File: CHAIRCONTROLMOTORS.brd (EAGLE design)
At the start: 110 x 115 mm, 57 parts, among them IC5 MCP2551, IC6 MCP2515, IC7 ATMEGA32U4NT-TQFP, J1 LEFT MOTOR, J10 XTXX-30F, J11 USB-B-PTH, J12 RoboClaw, J2 RIGHT MOTOR, J3 M01-2.5MM, J4 M01-2.5MM, J5 M01-2.5MM, J6 M01-2.5MM, J7 M01-2.5MM, J8 M01-2.5MM, J9 XTXX-30F, Q1 NTD5867NLT4G, Q2 NTD5867NLT4G

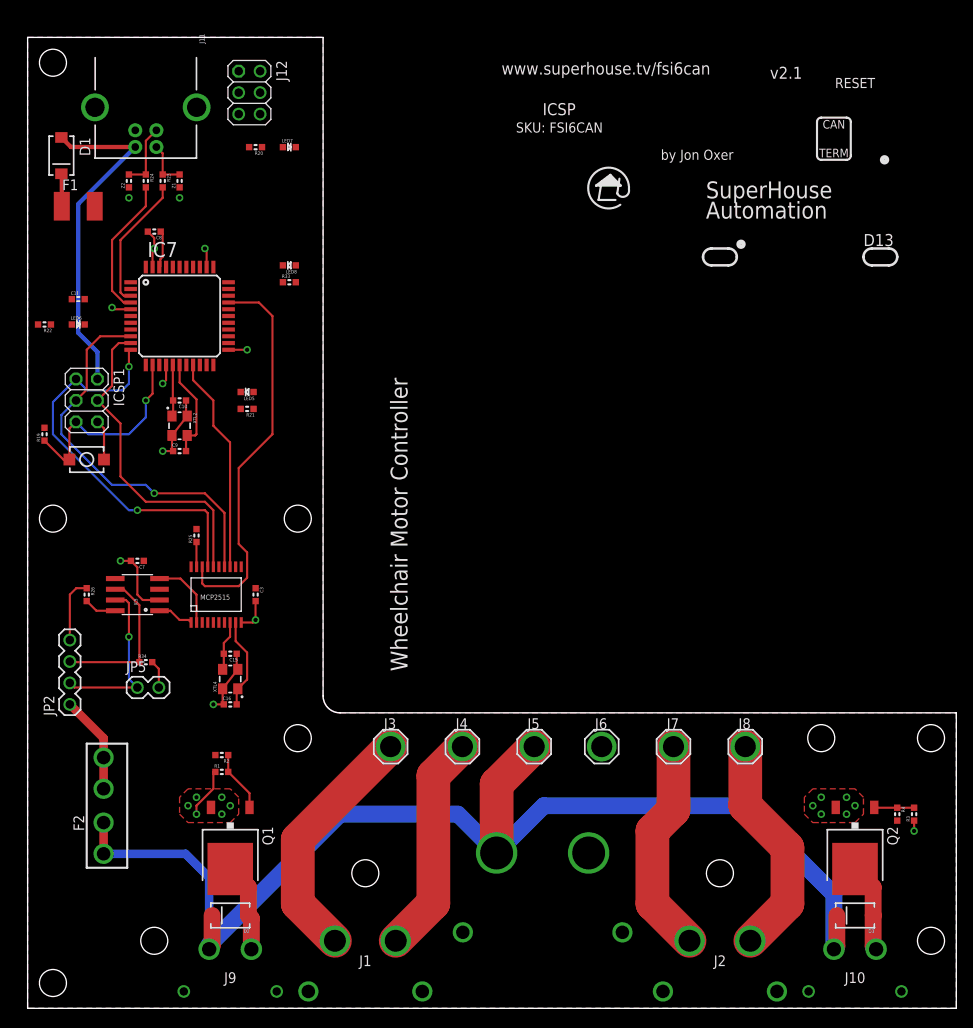
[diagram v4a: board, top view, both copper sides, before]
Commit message: Added brake status detection, finished routing
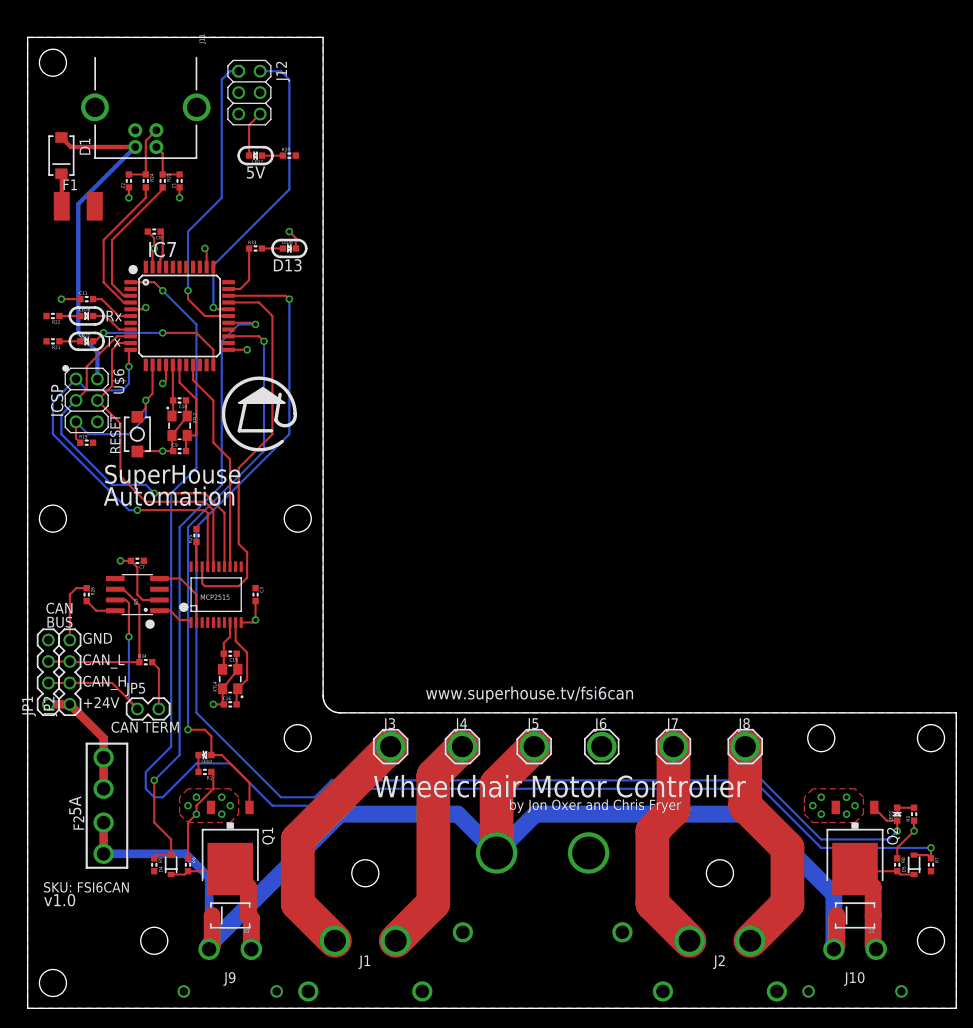
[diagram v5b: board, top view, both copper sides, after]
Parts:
- removed ICSP1: ICSP, pinhead:2X03
- removed R2, R4: 1K, SuperHouse-DiscreteSemi:R0603
- added D4, D5: (no value), SuperHouse-DiscreteSemi:SOD-323
- added JP1: CAN, SuperHouse-Connectors:1X04-P
- added LED1, LED2: (no value), SuperHouse-LEDs:LED-0603
- added R5, R7: 10K, SuperHouse-DiscreteSemi:R0603
- added R6, R8: 1K, SuperHouse-DiscreteSemi:R0603
- added U$6: ICSP-PIN, SuperHouse-Connectors:2X03-ICSP
- J10, J9: value XTXX-30F -> XT30F
- R1, R3: value 10K -> 1K
- moved R21 24.4 mm to (3.00, 79.0)
- moved LED5 19.9 mm to (7.00, 79.0), turned to 0 degrees
- moved S1 6.71 mm to (13.0, 68.0), turned to 90 degrees
- moved R33 5.66 mm to (27.0, 90.0)
- moved R19 5.10 mm to (7.00, 67.0), turned to 0 degrees
- moved LED7 4.12 mm to (27.0, 101.0), turned to 180 degrees
- moved R20 4.12 mm to (31.0, 101.0), turned to 0 degrees
- moved JP5 2.54 mm to (13.0, 35.5)
- moved LED8 2.00 mm to (31.0, 90.0), turned to 0 degrees
- moved R1 2.00 mm to (21.0, 28.0), turned to 180 degrees
- moved LED6 1.41 mm to (7.00, 82.0)
- moved R22 1.41 mm to (3.00, 82.0)
- moved C11 1.00 mm to (7.00, 84.0)
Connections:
- removed net LEFT_BRAKE_CONTROL: R2.2
- removed net N$4: Q2.1, R3.2, R4.1
- removed net RIGHT_BRAKE_CONTROL: R4.2
- new net N$5: LED1.C, R3.2
- net 5V: now also R5.2, R7.2
- net CANH: now also JP1.2
- net CANL: now also JP1.3
- net D4_A6: now also LED2.A, Q1.1
- net D5: now also LED1.A, Q2.1
- net D6_A8: now also D4.2, R5.1
- net D7_AIN0: now also D5.2, R7.1
- net GND: now also JP1.4, R6.1, R8.1, U$6.6; no longer ICSP1.6
- net LEFT_BRAKE: now also D4.1, R6.2
- net MISO: now also U$6.1; no longer ICSP1.1
- net MOSI: now also U$6.4; no longer ICSP1.4
- net N$1: now also LED2.C; no longer Q1.1, R2.1
- net N$2: now also JP1.1
- net RESET: now also U$6.5; no longer ICSP1.5
- net RIGHT_BRAKE: now also D5.1, R8.2
- net SCK: now also U$6.3; no longer ICSP1.3
- net USB+: now also U$6.2; no longer ICSP1.2
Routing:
- net D7_AIN0: track 0.00 -> 171.6 mm, vias 0 -> 2
- net D5: track 0.00 -> 156.9 mm, vias 0 -> 2
- net D6_A8: track 0.00 -> 75.3 mm, vias 0 -> 2
- net D4_A6: track 0.00 -> 68.3 mm, vias 0 -> 2
- net D9_A10: track 0.00 -> 36.5 mm, vias 0 -> 1
- net D8_A9: track 0.00 -> 35.7 mm, vias 0 -> 1
- net GND: track 62.0 -> 82.0 mm, vias 24 -> 26
- net TX_LED: track 0.00 -> 17.3 mm, vias 0 -> 2
- net LEFT_BRAKE: track 10.5 -> 18.5 mm
- net RIGHT_BRAKE: track 10.5 -> 18.5 mm
- net D13: track 0.00 -> 6.63 mm
- net CANH: track 20.4 -> 26.6 mm
- net 3V3: track 0.00 -> 5.27 mm
- net N$1: track 7.24 -> 2.00 mm
- net RXLED_SS: track 0.00 -> 5.10 mm
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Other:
- board text added: "+24V"
- board text added: "5A"
- board text added: "5V"
- board text added: "CAN BUS"
- board text added: "CAN TERM"
- board text added: "CAN_H"
- board text added: "CAN_L"
- board text added: "GND"
- board text added: "Rx"
- board text added: "Tx"
- board text added: "by Jon Oxer and Chris Fryer"
- board text added: "v1.0"
- board text removed: "CAN"
- board text removed: "TERM"
- board text removed: "by Jon Oxer"
- board text removed: "v2.1"

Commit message: Finished up silkscreen and routing
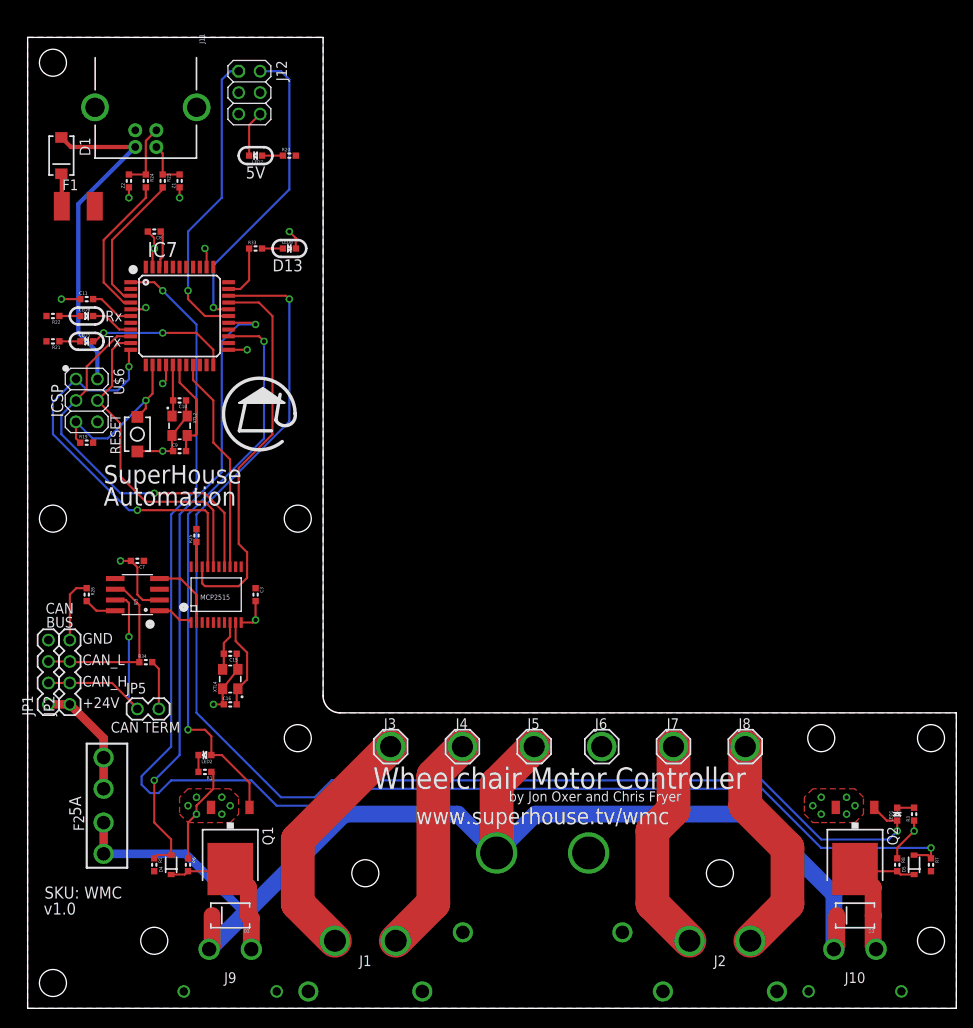
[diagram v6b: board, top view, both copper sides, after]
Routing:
- net 24V: track 143.3 -> 141.3 mm
- net D7_AIN0: track 171.6 -> 170.0 mm
- net RESET: track 21.3 -> 20.5 mm
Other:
- board text added: "(C)2019 SuperHouse Automation P/L"
- board text added: "SKU: WMC"
- board text added: "www.superhouse.tv/wmc"
- board text removed: "(C)2018-2019 SuperHouse Automation P/L"
- board text removed: "SKU: FSI6CAN"
- board text removed: "www.superhouse.tv/fsi6can"
